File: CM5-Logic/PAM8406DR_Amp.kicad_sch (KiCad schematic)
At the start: 8 parts, among them U1 PAM8406DR

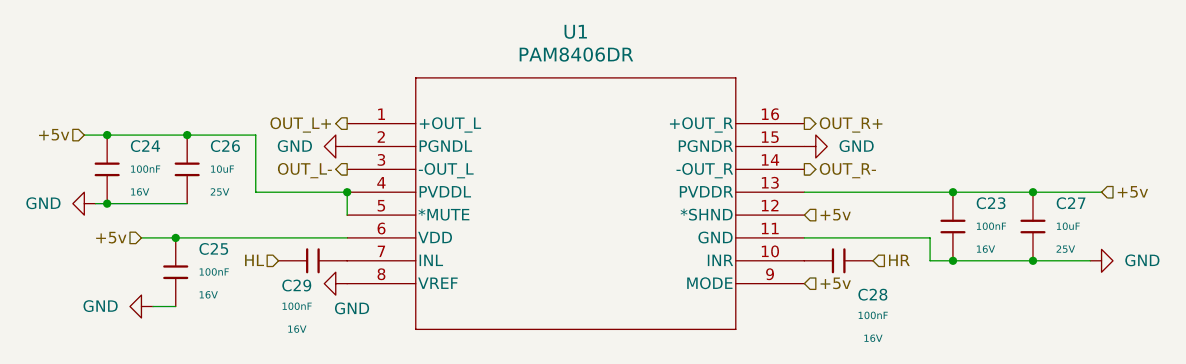
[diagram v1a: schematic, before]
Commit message: changes USB port, adds TMC2209 SilentStepStick footprint, redoes PCB Layout
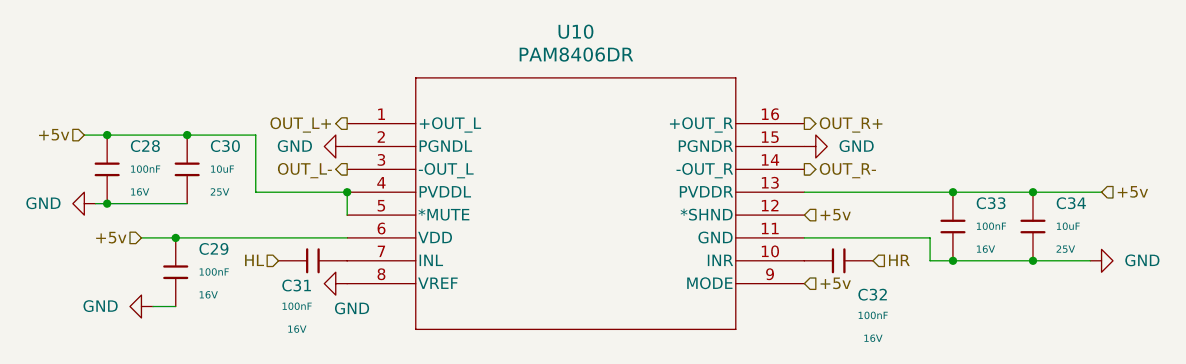
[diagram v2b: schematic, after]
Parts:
- renumbered C24 to C28, C25 to C29, C26 to C30, C29 to C31, C28 to C32, C23 to C33, C27 to C34, U1 to U10
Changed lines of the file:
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@@
 		(dnp no)
 		(fields_autoplaced yes)
-		(property "Reference" "C23"
+		(property "Reference" "C33"
 			(at 195.58 102.8699 0)
 			(effects
@@
 			(project "CM5IO"
 				(path "/e63e39d7-6ac0-4ffd-8aa3-1841a4541b55/423ee831-7c2f-4544-af8a-398bcd987f94"
-					(reference "C23")
+					(reference "C33")
 					(unit 1)
 				)
@@
 		(on_board yes)
 		(dnp no)
-		(property "Reference" "#PWR062"
+		(property "Reference" "#PWR070"
 			(at 91.44 102.87 0)
 			(effects
@@
 			(project "CM5IO"
 				(path "/e63e39d7-6ac0-4ffd-8aa3-1841a4541b55/423ee831-7c2f-4544-af8a-398bcd987f94"
-					(reference "#PWR062")
+					(reference "#PWR070")
 					(unit 1)
 				)
@@
 		(dnp no)
 		(fields_autoplaced yes)
-		(property "Reference" "#PWR028"
+		(property "Reference" "#PWR072"
 			(at 119.38 96.52 0)
 			(effects
@@
 			(project "CM5IO"
 				(path "/e63e39d7-6ac0-4ffd-8aa3-1841a4541b55/423ee831-7c2f-4544-af8a-398bcd987f94"
-					(reference "#PWR028")
+					(reference "#PWR072")
 					(unit 1)
 				)
@@
 		(dnp no)
 		(fields_autoplaced yes)
-		(property "Reference" "C25"
+		(property "Reference" "C29"
 			(at 109.22 107.9499 0)
 			(effects
@@
 			(project "CM5IO"
 				(path "/e63e39d7-6ac0-4ffd-8aa3-1841a4541b55/423ee831-7c2f-4544-af8a-398bcd987f94"
-					(reference "C25")
+					(reference "C29")
 					(unit 1)
 				)
@@
 		(dnp no)
 		(fields_autoplaced yes)
-		(property "Reference" "C26"
+		(property "Reference" "C30"
 			(at 110.49 96.5199 0)
 			(effects
@@
 			(project "CM5IO"
 				(path "/e63e39d7-6ac0-4ffd-8aa3-1841a4541b55/423ee831-7c2f-4544-af8a-398bcd987f94"
-					(reference "C26")
+					(reference "C30")
 					(unit 1)
 				)
@@
 		(on_board yes)
 		(dnp no)
-		(property "Reference" "#PWR057"
+		(property "Reference" "#PWR075"
 			(at 214.63 109.22 0)
 			(effects
@@
 			(project "CM5IO"
 				(path "/e63e39d7-6ac0-4ffd-8aa3-1841a4541b55/423ee831-7c2f-4544-af8a-398bcd987f94"
-					(reference "#PWR057")
+					(reference "#PWR075")
 					(unit 1)
 				)
@@
 		(dnp no)
 		(fields_autoplaced yes)
-		(property "Reference" "U1"
+		(property "Reference" "U10"
 			(at 151.13 83.82 0)
 			(effects
@@
 			(project "CM5IO"
 				(path "/e63e39d7-6ac0-4ffd-8aa3-1841a4541b55/423ee831-7c2f-4544-af8a-398bcd987f94"
-					(reference "U1")
+					(reference "U10")
 					(unit 1)
 				)
@@
 		(on_board yes)
 		(dnp no)
-		(property "Reference" "C29"
+		(property "Reference" "C31"
 			(at 120.142 112.014 90)
 			(effects
@@
 			(project "CM5IO"
 				(path "/e63e39d7-6ac0-4ffd-8aa3-1841a4541b55/423ee831-7c2f-4544-af8a-398bcd987f94"
-					(reference "C29")
+					(reference "C31")
 					(unit 1)
 				)
@@
 		(on_board yes)
 		(dnp no)
-		(property "Reference" "#PWR064"
+		(property "Reference" "#PWR071"
 			(at 97.79 114.3 0)
 			(effects
@@
 			(project "CM5IO"
 				(path "/e63e39d7-6ac0-4ffd-8aa3-1841a4541b55/423ee831-7c2f-4544-af8a-398bcd987f94"
-					(reference "#PWR064")
+					(reference "#PWR071")
 					(unit 1)
 				)
@@
 		(on_board yes)
 		(dnp no)
-		(property "Reference" "C28"
+		(property "Reference" "C32"
 			(at 184.15 113.03 90)
 			(effects
@@
 			(project "CM5IO"
 				(path "/e63e39d7-6ac0-4ffd-8aa3-1841a4541b55/423ee831-7c2f-4544-af8a-398bcd987f94"
-					(reference "C28")
+					(reference "C32")
 					(unit 1)
 				)
@@
 		(dnp no)
 		(fields_autoplaced yes)
-		(property "Reference" "C27"
+		(property "Reference" "C34"
 			(at 204.47 102.8699 0)
 			(effects
@@
 			(project "CM5IO"
 				(path "/e63e39d7-6ac0-4ffd-8aa3-1841a4541b55/423ee831-7c2f-4544-af8a-398bcd987f94"
-					(reference "C27")
+					(reference "C34")
 					(unit 1)
 				)
@@
 		(on_board yes)
 		(dnp no)
-		(property "Reference" "#PWR056"
+		(property "Reference" "#PWR074"
 			(at 182.88 96.52 0)
 			(effects
@@
 			(project "CM5IO"
 				(path "/e63e39d7-6ac0-4ffd-8aa3-1841a4541b55/423ee831-7c2f-4544-af8a-398bcd987f94"
-					(reference "#PWR056")
+					(reference "#PWR074")
 					(unit 1)
 				)
@@
 		(dnp no)
 		(fields_autoplaced yes)
-		(property "Reference" "C24"
+		(property "Reference" "C28"
 			(at 101.6 96.5199 0)
 			(effects
@@
 			(project "CM5IO"
 				(path "/e63e39d7-6ac0-4ffd-8aa3-1841a4541b55/423ee831-7c2f-4544-af8a-398bcd987f94"
-					(reference "C24")
+					(reference "C28")
 					(unit 1)
 				)
@@
 		(on_board yes)
 		(dnp no)
-		(property "Reference" "#PWR063"
+		(property "Reference" "#PWR073"
 			(at 119.38 111.76 0)
 			(effects
@@
 			(project "CM5IO"
 				(path "/e63e39d7-6ac0-4ffd-8aa3-1841a4541b55/423ee831-7c2f-4544-af8a-398bcd987f94"
-					(reference "#PWR063")
+					(reference "#PWR073")
 					(unit 1)
 				)
